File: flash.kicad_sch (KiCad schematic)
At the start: 13 parts, among them U10 IS25LP128F-JBLE

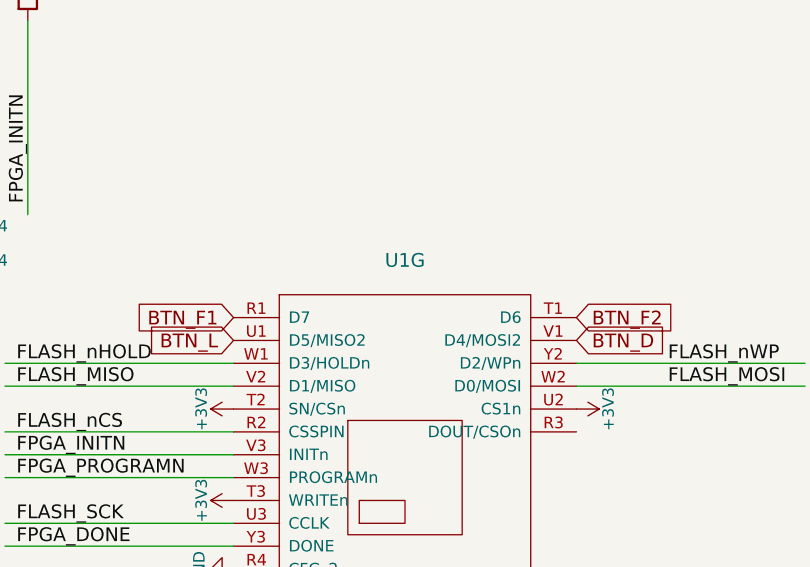
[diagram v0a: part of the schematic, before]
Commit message: Full SerDes is now connected
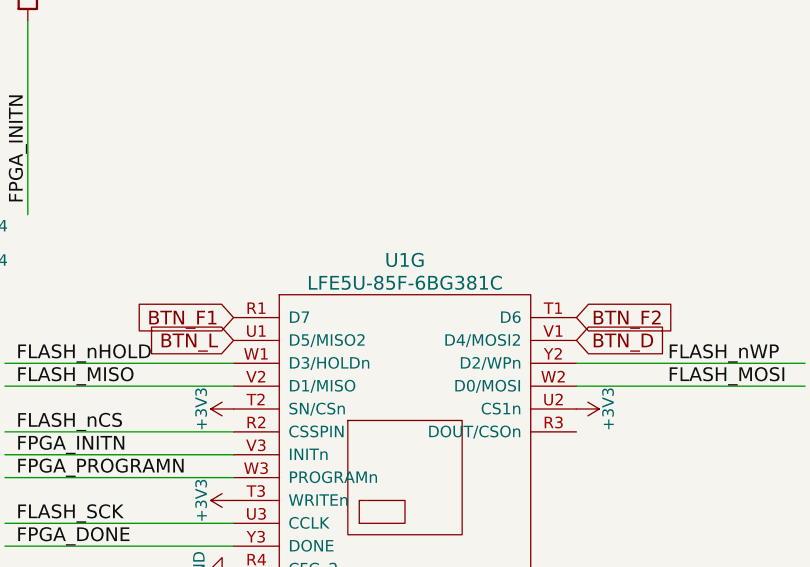
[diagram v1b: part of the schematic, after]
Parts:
- U1: value (none) -> LFE5U-85F-6BG381C; footprint (none) -> lfe5bg381:BGA-381_pitch0.8mm_dia0.4mm; MNF1_URL (none) -> www.latticesemi.com
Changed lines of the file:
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@@
   )
   (symbol (lib_id "lfe5bg381:LFE5UM-85F-6BG381C") (at 184.15 114.3 0) (unit 7)
-    (in_bom yes) (on_board yes)
+    (in_bom yes) (on_board no)
     (property "Reference" "U1" (id 0) (at 184.15 90.17 0)
       (effects (font (size 1.524 1.524)))
     )
-    (property "Value" "" (id 1) (at 184.15 92.71 0)
+    (property "Value" "LFE5U-85F-6BG381C" (id 1) (at 184.15 92.71 0)
       (effects (font (size 1.524 1.524)))
     )
-    (property "Footprint" "" (id 2) (at 157.48 90.17 0)
+    (property "Footprint" "lfe5bg381:BGA-381_pitch0.8mm_dia0.4mm" (id 2) (at 157.48 90.17 0)
       (effects (font (size 1.524 1.524)) hide)
     )
-    (property "Datasheet" "http://www.latticesemi.com/~/media/LatticeSemi/Documents/ApplicationNotes/EH/TN1260.pdf" (id 3) (at 157.48 90.17 0)
+    (property "Datasheet" "http://www.latticesemi.com/~/media/LatticeSemi/Documents/ApplicationNotes/EH/TN1261.pdf?document_id=50463" (id 3) (at 157.48 90.17 0)
       (effects (font (size 1.524 1.524)) hide)
     )
@@
       (effects (font (size 1.524 1.524)) hide)
     )
+    (property "MNF1_URL" "www.latticesemi.com" (id 5) (at 184.15 114.3 0)
+      (effects (font (size 1.524 1.524)) hide)
+    )
